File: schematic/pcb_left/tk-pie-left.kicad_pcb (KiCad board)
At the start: 2 copper layers, 150 x 77.5 mm, 34 parts, among them IC1 PCA9539PW,118, J1 NiceView Header, U3 SN74LVC1T45DCK

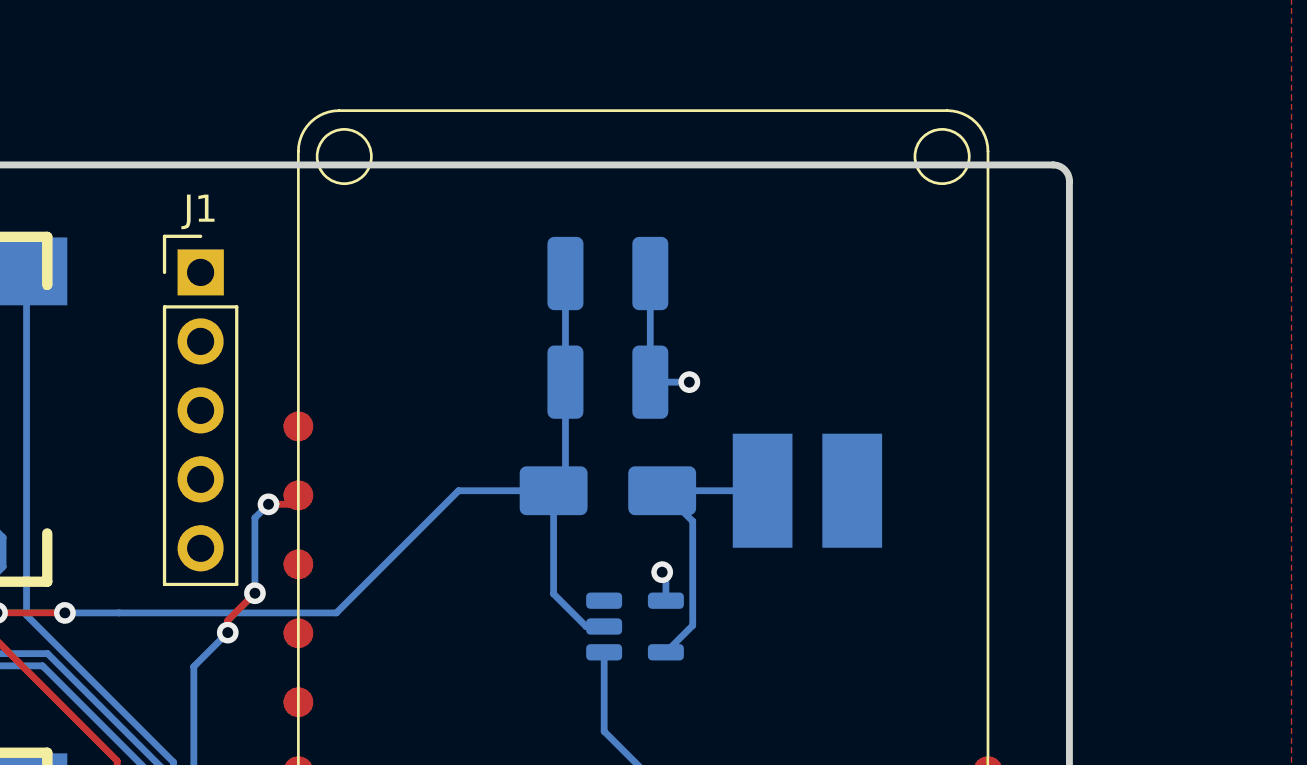
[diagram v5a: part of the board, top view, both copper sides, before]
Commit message: Add better niceview footprint
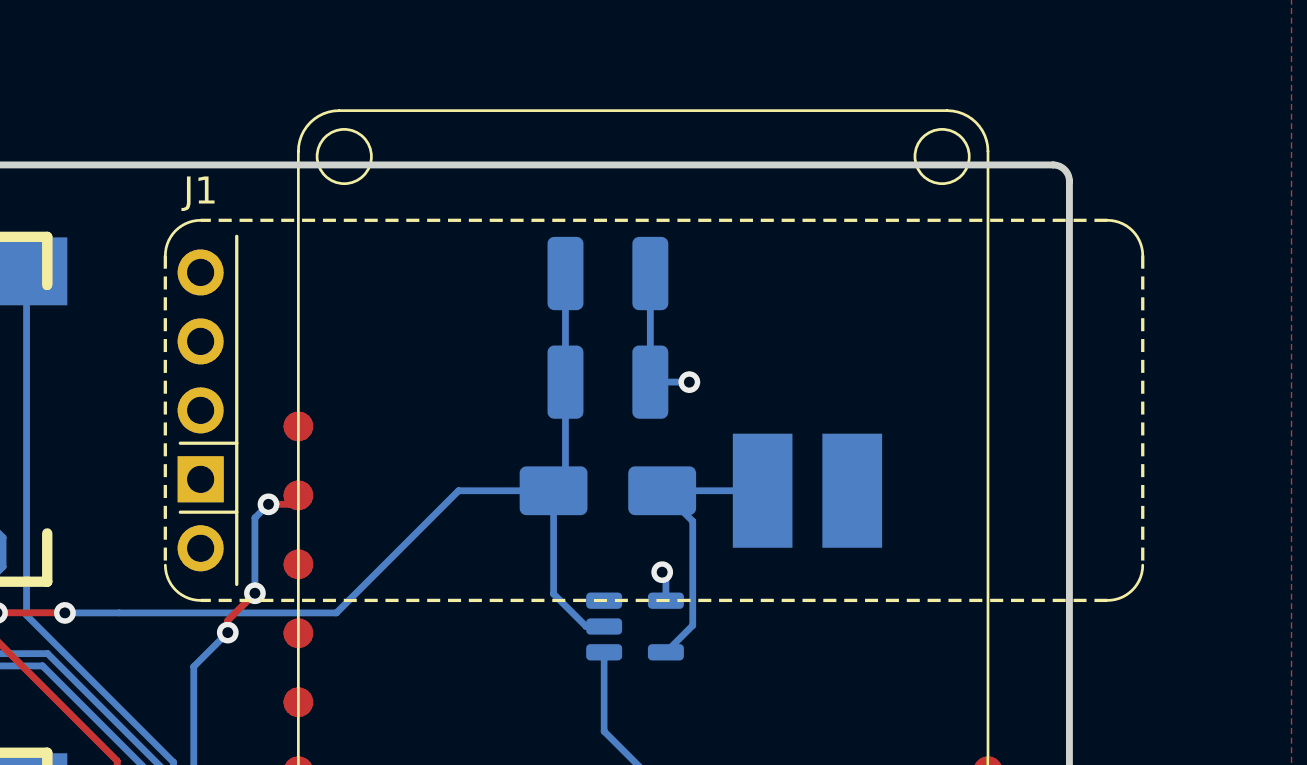
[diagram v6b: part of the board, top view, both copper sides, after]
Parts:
- J1: value NiceView Header -> NiceView; footprint Connector_PinHeader_2.54mm:PinHeader_1x05_P2.54mm_Vertical -> Footprints:Nice!View Header
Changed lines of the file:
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@@
 		)
 	)
-	(footprint "Connector_PinHeader_2.54mm:PinHeader_1x05_P2.54mm_Vertical"
+	(footprint "Footprints:Nice!View Header"
 		(layer "F.Cu")
 		(at 124 30.96)
@@
 		(tags "Through hole pin header THT 1x05 2.54mm single row")
 		(property "Reference" "J1"
-			(at 0 -2.33 0)
+			(at 0 -3 0)
 			(layer "F.SilkS")
 			(effects
@@
 			)
 		)
-		(property "Value" "NiceView Header"
+		(property "Value" "NiceView"
 			(at 0 12.49 0)
 			(layer "F.Fab")
@@
 			)
 		)
-		(property "Footprint" "Connector_PinHeader_2.54mm:PinHeader_1x05_P2.54mm_Vertical"
+		(property "Footprint" "Footprints:Nice!View Header"
 			(at 0 0 0)
 			(unlocked yes)
@@
 		(attr through_hole)
 		(fp_line
-			(start -1.33 -1.33)
-			(end 0 -1.33)
-			(stroke
-				(width 0.12)
-				(type solid)
-			)
-			(layer "F.SilkS")
-		)
-		(fp_line
-			(start -1.33 0)
-			(end -1.33 -1.33)
-			(stroke
-				(width 0.12)
-				(type solid)
-			)
-			(layer "F.SilkS")
-		)
-		(fp_line
-			(start -1.33 1.27)
-			(end -1.33 11.49)
-			(stroke
-				(width 0.12)
-				(type solid)
-			)
-			(layer "F.SilkS")
-		)
-		(fp_line
-			(start -1.33 1.27)
-			(end 1.33 1.27)
-			(stroke
-				(width 0.12)
-				(type solid)
-			)
-			(layer "F.SilkS")
-		)
-		(fp_line
-			(start -1.33 11.49)
+			(start -1.3 -0.62)
+			(end -1.3 10.78)
+			(stroke
+				(width 0.12)
+				(type dash)
+			)
+			(layer "F.SilkS")
+		)
+		(fp_line
+			(start -0.75 6.29)
+			(end 1.33 6.29)
+			(stroke
+				(width 0.12)
+				(type solid)
+			)
+			(layer "F.SilkS")
+		)
+		(fp_line
+			(start -0.75 8.83)
+			(end 1.33 8.83)
+			(stroke
+				(width 0.12)
+				(type solid)
+			)
+			(layer "F.SilkS")
+		)
+		(fp_line
+			(start 1.33 -1.33)
 			(end 1.33 11.49)
 			(stroke
@@
 		)
 		(fp_line
-			(start 1.33 1.27)
-			(end 1.33 11.49)
-			(stroke
-				(width 0.12)
-				(type solid)
+			(start 33.4 -1.92)
+			(end 0 -1.92)
+			(stroke
+				(width 0.12)
+				(type dash)
+			)
+			(layer "F.SilkS")
+		)
+		(fp_line
+			(start 33.4 12.08)
+			(end 0 12.08)
+			(stroke
+				(width 0.12)
+				(type dash)
+			)
+			(layer "F.SilkS")
+		)
+		(fp_line
+			(start 34.7 -0.62)
+			(end 34.7 10.78)
+			(stroke
+				(width 0.12)
+				(type dash)
+			)
+			(layer "F.SilkS")
+		)
+		(fp_arc
+			(start -1.3 -0.62)
+			(mid -0.919239 -1.539239)
+			(end 0 -1.92)
+			(stroke
+				(width 0.1)
+				(type default)
+			)
+			(layer "F.SilkS")
+		)
+		(fp_arc
+			(start 0 12.08)
+			(mid -0.919239 11.699239)
+			(end -1.3 10.78)
+			(stroke
+				(width 0.1)
+				(type default)
+			)
+			(layer "F.SilkS")
+		)
+		(fp_arc
+			(start 33.4 -1.92)
+			(mid 34.319239 -1.539239)
+			(end 34.7 -0.62)
+			(stroke
+				(width 0.1)
+				(type default)
+			)
+			(layer "F.SilkS")
+		)
+		(fp_arc
+			(start 34.7 10.78)
+			(mid 34.319239 11.699239)
+			(end 33.4 12.08)
+			(stroke
+				(width 0.1)
+				(type default)
 			)
 			(layer "F.SilkS")
@@
 			)
 		)
-		(pad "1" thru_hole rect
+		(pad "1" thru_hole oval
 			(at 0 0)
 			(size 1.7 1.7)
@@
 			(pintype "power_in")
 		)
-		(pad "4" thru_hole oval
+		(pad "4" thru_hole rect
 			(at 0 7.62)
 			(size 1.7 1.7)

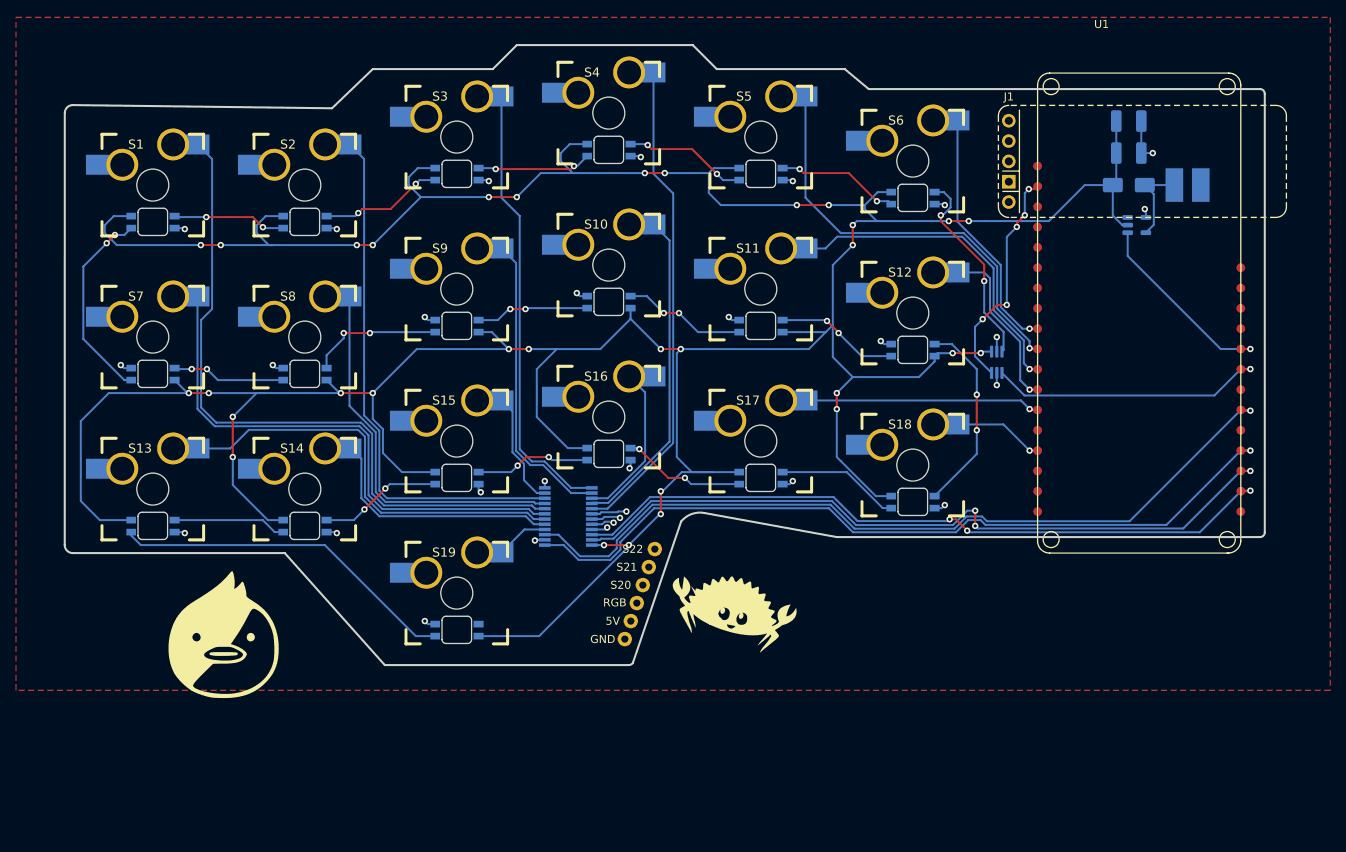
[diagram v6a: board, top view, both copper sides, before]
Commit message: Fix some schematic errors
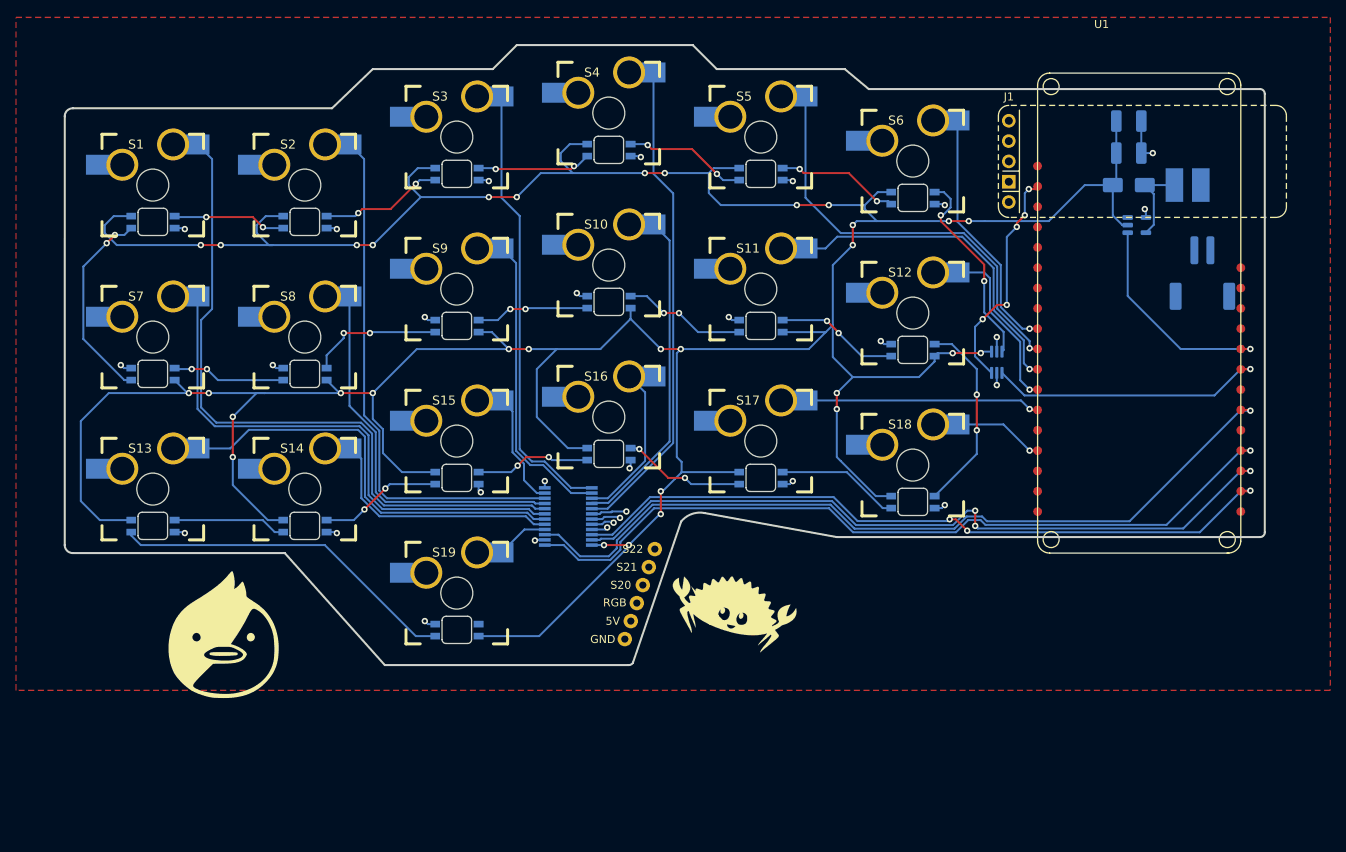
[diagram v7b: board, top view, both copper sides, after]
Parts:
- added REF**: JST_PH_S2B-PH-SM4-TB_1x02-1MP_P2.00mm_Horizontal, Connector_JST:JST_PH_S2B-PH-SM4-TB_1x02-1MP_P2.00mm_Horizontal, B.Cu at (148.2, 50.0)
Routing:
- net +5V: track 505.6 -> 502.1 mm
- net /5V_EN: track 24.3 -> 27.2 mm
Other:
- outline, holes or cut-outs redrawn

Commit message: More schematics
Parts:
- removed REF**: JST_PH_S2B-PH-SM4-TB_1x02-1MP_P2.00mm_Horizontal, Connector_JST:JST_PH_S2B-PH-SM4-TB_1x02-1MP_P2.00mm_Horizontal
- added J2: Battery Connector, Connector_JST:JST_PH_S2B-PH-SM4-TB_1x02-1MP_P2.00mm_Horizontal, B.Cu at (147.1, 47.8)
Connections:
- J1 pad 1: unconnected-(J1-MOSI-Pad1) -> /NV_MOSI
- J1 pad 2: unconnected-(J1-SCK-Pad2) -> /NV_SCK
- J1 pad 3: unconnected-(J1-VCC-Pad3) -> +3.3V
- J1 pad 4: unconnected-(J1-GND-Pad4) -> GND
- J1 pad 5: unconnected-(J1-CS-Pad5) -> / NV_CS
- L2 pad 1: Vbat -> /VBAT
- U1 pad 21: unconnected-(U1-DAT1-Pad21) -> /NV_MOSI
- U1 pad 22: unconnected-(U1-DAT2-Pad22) -> /NV_SCK
- U1 pad 23: unconnected-(U1-DAT3-Pad23) -> / NV_CS
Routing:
- net /NV_MOSI: track 0.00 -> 27.6 mm, vias 0 -> 1
- net /NV_SCK: track 0.00 -> 22.1 mm, vias 0 -> 1
- net Net-(E3-Pin_1): track 0.00 -> 20.9 mm, vias 0 -> 1
- net /S20: track 2.91 -> 13.1 mm
- net / NV_CS: track 0.00 -> 9.70 mm
- net +5V: track 502.1 -> 509.9 mm, vias 32 -> 34
- net /S21: track 3.69 -> 11.3 mm
- net /S22: track 4.45 -> 10.6 mm
- net /VBAT: track 0.00 -> 5.95 mm
- net +3.3V: track 28.6 -> 33.6 mm
- net GND: track 39.9 -> 44.3 mm, vias 26 -> 27
